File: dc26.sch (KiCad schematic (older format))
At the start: 50 parts, among them J1 CONN_01X10, J2 CONN_01X10, J3 CONN_01X10, Y1 Crystal

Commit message: Pads for unused pins
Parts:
- removed CON_PWR1: CONN_01X02, Pin_Headers:Pin_Header_Angled_1x02_Pitch2.54mm, symbol CONN_01X02
- removed J1, J2: CONN_01X10, Pin_Headers:Pin_Header_Angled_1x10_Pitch2.00mm, symbol CONN_01X10
- added IRRXF1: IRRXF, Measurement_Points:Measurement_Point_Round-SMD-Pad_Small, symbol TEST
- added IRTXF1: IRTXF, Measurement_Points:Measurement_Point_Round-SMD-Pad_Small, symbol TEST
- added PC0: PC0, Measurement_Points:Measurement_Point_Round-SMD-Pad_Small, symbol TEST
- added PC1: PC1, Measurement_Points:Measurement_Point_Round-SMD-Pad_Small, symbol TEST
- added PC12: PC12, Measurement_Points:Measurement_Point_Round-SMD-Pad_Small, symbol TEST
- added PC13: PC13, Measurement_Points:Measurement_Point_Round-SMD-Pad_Small, symbol TEST
- added PC14: PC14, Measurement_Points:Measurement_Point_Round-SMD-Pad_Small, symbol TEST
- added PC15: PC15, Measurement_Points:Measurement_Point_Round-SMD-Pad_Small, symbol TEST
- added PC2: PC2, Measurement_Points:Measurement_Point_Round-SMD-Pad_Small, symbol TEST
- added PC3: PC3, Measurement_Points:Measurement_Point_Round-SMD-Pad_Small, symbol TEST
- added PC4: PC4, Measurement_Points:Measurement_Point_Round-SMD-Pad_Small, symbol TEST
- added PC5: PC5, Measurement_Points:Measurement_Point_Round-SMD-Pad_Small, symbol TEST
- added PC6: PC6, Measurement_Points:Measurement_Point_Round-SMD-Pad_Small, symbol TEST
- added PC7: PC7, Measurement_Points:Measurement_Point_Round-SMD-Pad_Small, symbol TEST
- added PC8: PC8, Measurement_Points:Measurement_Point_Round-SMD-Pad_Small, symbol TEST
- added PC9: PC9, Measurement_Points:Measurement_Point_Round-SMD-Pad_Small, symbol TEST
- SW_BOOT0, SW_RESET1: footprint Buttons_Switches_SMD:SW_SPST_EVQQ2 -> Buttons_Switches_SMD:SW_SPST_EVQPE1
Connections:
- net labels removed: VCC
- wire segments 207 -> 215

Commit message: voltage divider
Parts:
- removed PC12: PC12, Measurement_Points:Measurement_Point_Round-SMD-Pad_Small, symbol TEST
- removed PC13: PC13, Measurement_Points:Measurement_Point_Round-SMD-Pad_Small, symbol TEST
- removed PC14: PC14, Measurement_Points:Measurement_Point_Round-SMD-Pad_Small, symbol TEST
- removed PC15: PC15, Measurement_Points:Measurement_Point_Round-SMD-Pad_Small, symbol TEST
- removed PC9: PC9, Measurement_Points:Measurement_Point_Round-SMD-Pad_Small, symbol TEST
- added C?: 0.1uF, Capacitors_SMD:C_0603, symbol C_Small
- added VBAT-DIV1: 5k-10k, TO_SOT_Packages_SMD:SOT-23, symbol Voltage_Divider
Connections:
- net labels added: +BATT
- wire segments 215 -> 212
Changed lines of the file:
@@
-$EndComp
-$Comp
-L TEST PC9
-U 1 1 5B18EB92
-P -11550 8450
-F 0 "PC9" H -11550 8750 50  0000 C BNN
-F 1 "PC9" H -11550 8700 50  0000 C CNN
-F 2 "Measurement_Points:Measurement_Point_Round-SMD-Pad_Small" H -11550 8450 50  0001 C CNN
-F 3 "" H -11550 8450 50  0001 C CNN
-	1    -11550 8450
-	-1   0    0    1
 $EndComp
 $Comp
@@
 	-1   0    0    1
 $EndComp
-$Comp
-L TEST PC12
-U 1 1 5B18EDE3
-P -12000 8900
-F 0 "PC12" H -12000 9200 50  0000 C BNN
-F 1 "PC12" H -12000 9150 50  0000 C CNN
-F 2 "Measurement_Points:Measurement_Point_Round-SMD-Pad_Small" H -12000 8900 50  0001 C CNN
-F 3 "" H -12000 8900 50  0001 C CNN
-	1    -12000 8900
-	-1   0    0    1
-$EndComp
-$Comp
-L TEST PC13
-U 1 1 5B18EEAC
-P -12150 9050
-F 0 "PC13" H -12150 9350 50  0000 C BNN
-F 1 "PC13" H -12150 9300 50  0000 C CNN
-F 2 "Measurement_Points:Measurement_Point_Round-SMD-Pad_Small" H -12150 9050 50  0001 C CNN
-F 3 "" H -12150 9050 50  0001 C CNN
-	1    -12150 9050
-	-1   0    0    1
-$EndComp
-$Comp
-L TEST PC14
-U 1 1 5B18EF78
-P -12300 9200
-F 0 "PC14" H -12300 9500 50  0000 C BNN
-F 1 "PC14" H -12300 9450 50  0000 C CNN
-F 2 "Measurement_Points:Measurement_Point_Round-SMD-Pad_Small" H -12300 9200 50  0001 C CNN
-F 3 "" H -12300 9200 50  0001 C CNN
-	1    -12300 9200
-	-1   0    0    1
-$EndComp
-$Comp
-L TEST PC15
-U 1 1 5B18F04B
-P -12450 9350
-F 0 "PC15" H -12450 9650 50  0000 C BNN
-F 1 "PC15" H -12450 9600 50  0000 C CNN
-F 2 "Measurement_Points:Measurement_Point_Round-SMD-Pad_Small" H -12450 9350 50  0001 C CNN
-F 3 "" H -12450 9350 50  0001 C CNN
-	1    -12450 9350
-	-1   0    0    1
-$EndComp
 Wire Wire Line
 	-4700 -6350 -3700 -6350
@@
 	-2500 -5700 -3500 -5700
 Wire Wire Line
-	-3500 -4900 -3500 -5700
-Wire Wire Line
-	-4700 -4900 -3500 -4900
+	-3500 -5700 -3500 -4900
+Wire Wire Line
+	-3500 -4900 -4700 -4900
 Wire Wire Line
 	-2500 -5600 -3400 -5600
 Wire Wire Line
-	-3400 -4650 -3400 -5600
-Wire Wire Line
-	-4700 -4650 -3400 -4650
+	-3400 -5600 -3400 -4650
+Wire Wire Line
+	-3400 -4650 -4700 -4650
 Wire Wire Line
 	-2500 -5500 -3350 -5500
 Wire Wire Line
-	-3350 -4400 -3350 -5500
-Wire Wire Line
-	-4700 -4400 -3350 -4400
+	-3350 -5500 -3350 -4400
+Wire Wire Line
+	-3350 -4400 -4700 -4400
 Wire Wire Line
 	-2500 -4650 -3300 -4650
 Wire Wire Line
-	-3300 -4000 -3300 -4650
-Wire Wire Line
-	-4700 -4000 -3300 -4000
+	-3300 -4650 -3300 -4000
+Wire Wire Line
+	-3300 -4000 -4700 -4000
 Wire Wire Line
 	-2500 -4550 -3250 -4550
 Wire Wire Line
-	-3250 -3750 -3250 -4550
-Wire Wire Line
-	-4700 -3750 -3250 -3750
+	-3250 -4550 -3250 -3750
+Wire Wire Line
+	-3250 -3750 -4700 -3750
 Wire Wire Line
 	-5650 -6600 -5650 -3750
@@
 	-2100 6950 -2100 4050
 Wire Wire Line
-	-3050 4050 -2100 4050
-Wire Wire Line
-	-3050 -2850 -3050 4050
-Wire Wire Line
-	-2900 -2850 -3050 -2850
+	-2100 4050 -3050 4050
+Wire Wire Line
+	-3050 4050 -3050 -2850
+Wire Wire Line
+	-3050 -2850 -2900 -2850
 Wire Wire Line
 	-2700 7750 850  7750
@@
 	-11300 5950 -12250 5950
 Wire Wire Line
-	-12250 5850 -12250 5950
-Wire Wire Line
-	-13650 5850 -12250 5850
+	-12250 5950 -12250 5850
+Wire Wire Line
+	-12250 5850 -13650 5850
 Wire Wire Line
 	-11300 6050 -12250 6050
 Wire Wire Line
-	-12250 6150 -12250 6050
-Wire Wire Line
-	-13650 6150 -12250 6150
+	-12250 6050 -12250 6150
+Wire Wire Line
+	-12250 6150 -13650 6150
 Wire Wire Line
 	-13400 6250 -13400 5850
@@
 Connection ~ -11750 7150
 Wire Wire Line
-	-12450 9350 -12450 7950
-Wire Wire Line
-	-12300 9200 -12300 7850
-Connection ~ -12300 7850
-Wire Wire Line
-	-12150 9050 -12150 7750
-Connection ~ -12150 7750
-Wire Wire Line
-	-12000 8900 -12000 7650
-Connection ~ -12000 7650
-Wire Wire Line
 	-11850 8750 -11850 7550
 Connection ~ -11850 7550
 Wire Wire Line
 	-11700 8600 -11700 7450
-Connection ~ -11700 7450
-Wire Wire Line
-	-11550 8450 -11550 7350
-Connection ~ -11550 7350
 Wire Wire Line
 	-11400 8300 -11400 7250
 Connection ~ -11400 7250
+Connection ~ -11700 7450
+$Comp
+L Voltage_Divider VBAT-DIV1
+U 1 1 5B15AEF3
+P -250 6550
+F 0 "VBAT-DIV1" V -425 6550 50  0000 C CNN
+F 1 "5k-10k" V -350 6550 50  0000 C CNN
+F 2 "TO_SOT_Packages_SMD:SOT-23" V 225 6550 50  0001 C CNN
+F 3 "" H -50 6550 50  0001 C CNN
+	1    -250 6550
+	-1   0    0    1
+$EndComp
+Wire Wire Line
+	-2700 6550 -400 6550
+$Comp
+L GND #PWR?
+U 1 1 5B15B26B
+P -250 6800
+F 0 "#PWR?" H -250 6550 50  0001 C CNN
+F 1 "GND" H -250 6650 50  0000 C CNN
+F 2 "" H -250 6800 50  0001 C CNN
+F 3 "" H -250 6800 50  0001 C CNN
+	1    -250 6800
+	1    0    0    -1
+$EndComp
+$Comp
+L +BATT #PWR?
+U 1 1 5B15B508
+P -250 6300
+F 0 "#PWR?" H -250 6150 50  0001 C CNN
+F 1 "+BATT" H -250 6440 50  0000 C CNN
+F 2 "" H -250 6300 50  0001 C CNN
+F 3 "" H -250 6300 50  0001 C CNN
+	1    -250 6300
+	1    0    0    -1
+$EndComp
+$Comp
+L GND #PWR?
+U 1 1 5B15BD01
+P -900 6800
+F 0 "#PWR?" H -900 6550 50  0001 C CNN
+F 1 "GND" H -900 6650 50  0000 C CNN
+F 2 "" H -900 6800 50  0001 C CNN
+F 3 "" H -900 6800 50  0001 C CNN
+	1    -900 6800
+	1    0    0    -1
+$EndComp
+$Comp
+L C_Small C?
+U 1 1 5B15C038
+P -900 6700
+F 0 "C?" H -890 6770 50  0000 L CNN
+F 1 "0.1uF" H -890 6620 50  0000 L CNN
+F 2 "Capacitors_SMD:C_0603" H -900 6700 50  0001 C CNN
+F 3 "" H -900 6700 50  0001 C CNN
+	1    -900 6700
+	1    0    0    -1
+$EndComp
+Wire Wire Line
+	-900 6550 -900 6600
+Connection ~ -900 6550
 $EndSCHEMATC

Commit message: Fixed up some mess + IR + USB new footprint + buttons
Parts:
- removed J3: CONN_01X10, Pin_Headers:Pin_Header_Angled_1x10_Pitch2.00mm, symbol CONN_01X10
- gave numbers to parts that had none: 1
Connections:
- wire segments 212 -> 209
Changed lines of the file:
@@
 $EndComp
 $Comp
-L GND #PWR14
+L GND #PWR12
 U 1 1 5AD27FBE
 P -3450 -6450
-F 0 "#PWR14" H -3450 -6700 50  0001 C CNN
+F 0 "#PWR12" H -3450 -6700 50  0001 C CNN
 F 1 "GND" H -3450 -6600 50  0000 C CNN
 F 2 "" H -3450 -6450 50  0001 C CNN
@@
 $EndComp
 $Comp
-L GND #PWR15
+L GND #PWR13
 U 1 1 5AD6E593
 P -2500 -5100
-F 0 "#PWR15" H -2500 -5350 50  0001 C CNN
+F 0 "#PWR13" H -2500 -5350 50  0001 C CNN
 F 1 "GND" H -2500 -5250 50  0000 C CNN
 F 2 "" H -2500 -5100 50  0001 C CNN
@@
 $EndComp
 $Comp
-L GND #PWR16
+L GND #PWR14
 U 1 1 5AD6F999
 P -2500 -3550
-F 0 "#PWR16" H -2500 -3800 50  0001 C CNN
+F 0 "#PWR14" H -2500 -3800 50  0001 C CNN
 F 1 "GND" H -2500 -3700 50  0000 C CNN
 F 2 "" H -2500 -3550 50  0001 C CNN
@@
 $EndComp
 $Comp
-L GND #PWR13
+L GND #PWR11
 U 1 1 5AD77A72
 P -3600 -800
-F 0 "#PWR13" H -3600 -1050 50  0001 C CNN
+F 0 "#PWR11" H -3600 -1050 50  0001 C CNN
 F 1 "GND" H -3600 -950 50  0000 C CNN
 F 2 "" H -3600 -800 50  0001 C CNN
@@
 $EndComp
 $Comp
-L GND #PWR10
+L GND #PWR8
 U 1 1 5B04F2A2
 P -7000 8800
-F 0 "#PWR10" H -7000 8550 50  0001 C CNN
+F 0 "#PWR8" H -7000 8550 50  0001 C CNN
 F 1 "GND" H -7000 8650 50  0000 C CNN
 F 2 "" H -7000 8800 50  0001 C CNN
@@
 $EndComp
 $Comp
-L +3.3V #PWR9
+L +3.3V #PWR7
 U 1 1 5B0D3E01
 P -7200 2050
-F 0 "#PWR9" H -7200 1900 50  0001 C CNN
+F 0 "#PWR7" H -7200 1900 50  0001 C CNN
 F 1 "+3.3V" H -7200 2190 50  0000 C CNN
 F 2 "" H -7200 2050 50  0001 C CNN
@@
 $EndComp
 $Comp
-L GND #PWR7
+L GND #PWR5
 U 1 1 5B0F137D
 P -12250 5250
-F 0 "#PWR7" H -12250 5000 50  0001 C CNN
+F 0 "#PWR5" H -12250 5000 50  0001 C CNN
 F 1 "GND" H -12250 5100 50  0000 C CNN
 F 2 "" H -12250 5250 50  0001 C CNN
@@
 $EndComp
 $Comp
-L GND #PWR11
+L GND #PWR9
 U 1 1 5B0F6A9C
 P -6200 3750
-F 0 "#PWR11" H -6200 3500 50  0001 C CNN
+F 0 "#PWR9" H -6200 3500 50  0001 C CNN
 F 1 "GND" H -6200 3600 50  0000 C CNN
 F 2 "" H -6200 3750 50  0001 C CNN
@@
 $EndComp
 $Comp
-L +3.3V #PWR8
+L +3.3V #PWR6
 U 1 1 5B11C638
 P -11750 3950
-F 0 "#PWR8" H -11750 3800 50  0001 C CNN
+F 0 "#PWR6" H -11750 3800 50  0001 C CNN
 F 1 "+3.3V" H -11750 4090 50  0000 C CNN
 F 2 "" H -11750 3950 50  0001 C CNN
@@
 $EndComp
 $Comp
-L GND #PWR5
+L GND #PWR4
 U 1 1 5B12677B
 P -12400 4350
-F 0 "#PWR5" H -12400 4100 50  0001 C CNN
+F 0 "#PWR4" H -12400 4100 50  0001 C CNN
 F 1 "GND" H -12400 4200 50  0000 C CNN
 F 2 "" H -12400 4350 50  0001 C CNN
@@
 $EndComp
 $Comp
-L GND #PWR4
+L GND #PWR3
 U 1 1 5B1309D3
 P -12450 4950
-F 0 "#PWR4" H -12450 4700 50  0001 C CNN
+F 0 "#PWR3" H -12450 4700 50  0001 C CNN
 F 1 "GND" H -12450 4800 50  0000 C CNN
 F 2 "" H -12450 4950 50  0001 C CNN
@@
 $EndComp
 $Comp
-L +3.3V #PWR3
+L +3.3V #PWR2
 U 1 1 5B136E3C
 P -12450 4750
-F 0 "#PWR3" H -12450 4600 50  0001 C CNN
+F 0 "#PWR2" H -12450 4600 50  0001 C CNN
 F 1 "+3.3V" H -12450 4890 50  0000 C CNN
 F 2 "" H -12450 4750 50  0001 C CNN
@@
 $EndComp
 $Comp
-L GND #PWR17
+L GND #PWR15
 U 1 1 5B13B631
 P -1800 6650
-F 0 "#PWR17" H -1800 6400 50  0001 C CNN
+F 0 "#PWR15" H -1800 6400 50  0001 C CNN
 F 1 "GND" H -1800 6500 50  0000 C CNN
 F 2 "" H -1800 6650 50  0001 C CNN
@@
 $EndComp
 $Comp
-L GND #PWR18
+L GND #PWR16
 U 1 1 5B1B7467
 P -1200 9050
-F 0 "#PWR18" H -1200 8800 50  0001 C CNN
+F 0 "#PWR16" H -1200 8800 50  0001 C CNN
 F 1 "GND" H -1200 8900 50  0000 C CNN
 F 2 "" H -1200 9050 50  0001 C CNN
@@
 $EndComp
 $Comp
-L +5V #PWR12
+L +5V #PWR10
 U 1 1 5B123F56
 P -5650 -6600
-F 0 "#PWR12" H -5650 -6750 50  0001 C CNN
+F 0 "#PWR10" H -5650 -6750 50  0001 C CNN
 F 1 "+5V" H -5650 -6460 50  0000 C CNN
 F 2 "" H -5650 -6600 50  0001 C CNN
@@
 LED-POWER-ENABLE
 $Comp
-L GND #PWR22
+L GND #PWR20
 U 1 1 5B188D2F
 P -1100 -5650
-F 0 "#PWR22" H -1100 -5900 50  0001 C CNN
+F 0 "#PWR20" H -1100 -5900 50  0001 C CNN
 F 1 "GND" H -1100 -5800 50  0000 C CNN
 F 2 "" H -1100 -5650 50  0001 C CNN
@@
 $EndComp
 $Comp
-L +5V #PWR21
+L +5V #PWR19
 U 1 1 5B1896AE
 P -1100 -5850
-F 0 "#PWR21" H -1100 -6000 50  0001 C CNN
+F 0 "#PWR19" H -1100 -6000 50  0001 C CNN
 F 1 "+5V" H -1100 -5710 50  0000 C CNN
 F 2 "" H -1100 -5850 50  0001 C CNN
@@
 $EndComp
 $Comp
-L +5V #PWR19
+L +5V #PWR17
 U 1 1 5B189C3C
 P -1150 -4300
-F 0 "#PWR19" H -1150 -4450 50  0001 C CNN
+F 0 "#PWR17" H -1150 -4450 50  0001 C CNN
 F 1 "+5V" H -1150 -4160 50  0000 C CNN
 F 2 "" H -1150 -4300 50  0001 C CNN
@@
 $EndComp
 $Comp
-L GND #PWR20
+L GND #PWR18
 U 1 1 5B189D37
 P -1150 -4150
-F 0 "#PWR20" H -1150 -4400 50  0001 C CNN
+F 0 "#PWR18" H -1150 -4400 50  0001 C CNN
 F 1 "GND" H -1150 -4300 50  0000 C CNN
 F 2 "" H -1150 -4150 50  0001 C CNN
@@
 IR-TX-F
 $Comp
-L CONN_01X10 J3
-U 1 1 5B13C46C
-P 1050 7500
-F 0 "J3" H 1050 8050 50  0000 C CNN
-F 1 "CONN_01X10" V 1150 7500 50  0000 C CNN
-F 2 "Pin_Headers:Pin_Header_Angled_1x10_Pitch2.00mm" H 1050 7500 50  0001 C CNN
-F 3 "" H 1050 7500 50  0001 C CNN
-	1    1050 7500
-	1    0    0    -1
-$EndComp
-$Comp
 L TEST PC0
 U 1 1 5B18C803
@@
 	-13250 7450 -11300 7450
 Wire Wire Line
-	-2700 7850 850  7850
-Wire Wire Line
-	-2700 7650 850  7650
-Wire Wire Line
 	-2700 7550 850  7550
 Wire Wire Line
 	-2700 7450 850  7450
-Wire Wire Line
-	-2700 7350 850  7350
 Wire Wire Line
 	-2700 7250 850  7250
@@
 	-2700 6550 -400 6550
 $Comp
-L GND #PWR?
+L GND #PWR23
 U 1 1 5B15B26B
 P -250 6800
-F 0 "#PWR?" H -250 6550 50  0001 C CNN
+F 0 "#PWR23" H -250 6550 50  0001 C CNN
 F 1 "GND" H -250 6650 50  0000 C CNN
 F 2 "" H -250 6800 50  0001 C CNN
@@
 $EndComp
 $Comp
-L +BATT #PWR?
+L +BATT #PWR22
 U 1 1 5B15B508
 P -250 6300
-F 0 "#PWR?" H -250 6150 50  0001 C CNN
+F 0 "#PWR22" H -250 6150 50  0001 C CNN
 F 1 "+BATT" H -250 6440 50  0000 C CNN
 F 2 "" H -250 6300 50  0001 C CNN
@@
 $EndComp
 $Comp
-L GND #PWR?
+L GND #PWR21
 U 1 1 5B15BD01
 P -900 6800
-F 0 "#PWR?" H -900 6550 50  0001 C CNN
+F 0 "#PWR21" H -900 6550 50  0001 C CNN
 F 1 "GND" H -900 6650 50  0000 C CNN
 F 2 "" H -900 6800 50  0001 C CNN
@@
 $EndComp
 $Comp
-L C_Small C?
+L C_Small C2
 U 1 1 5B15C038
 P -900 6700
-F 0 "C?" H -890 6770 50  0000 L CNN
+F 0 "C2" H -890 6770 50  0000 L CNN
 F 1 "0.1uF" H -890 6620 50  0000 L CNN
 F 2 "Capacitors_SMD:C_0603" H -900 6700 50  0001 C CNN

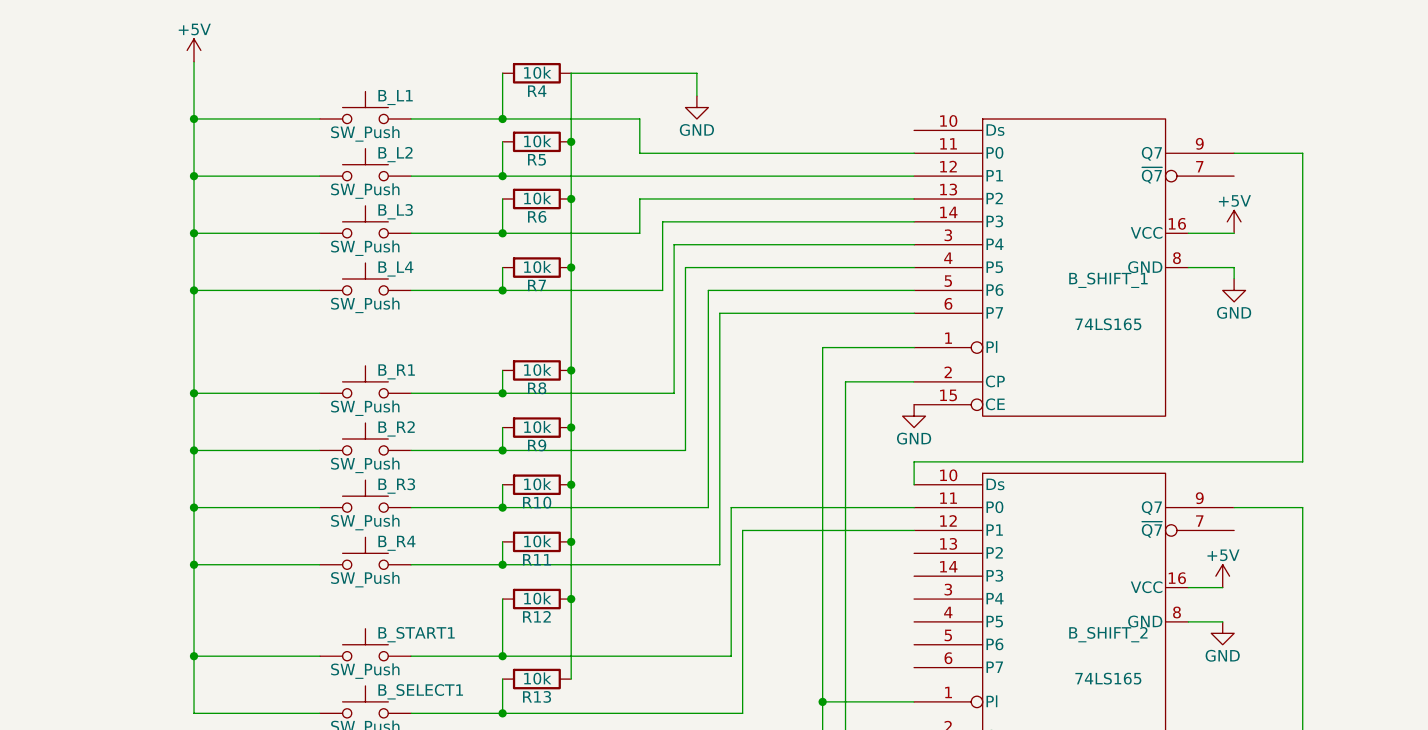
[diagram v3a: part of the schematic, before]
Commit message: clean up and moved shifters to 3.3v
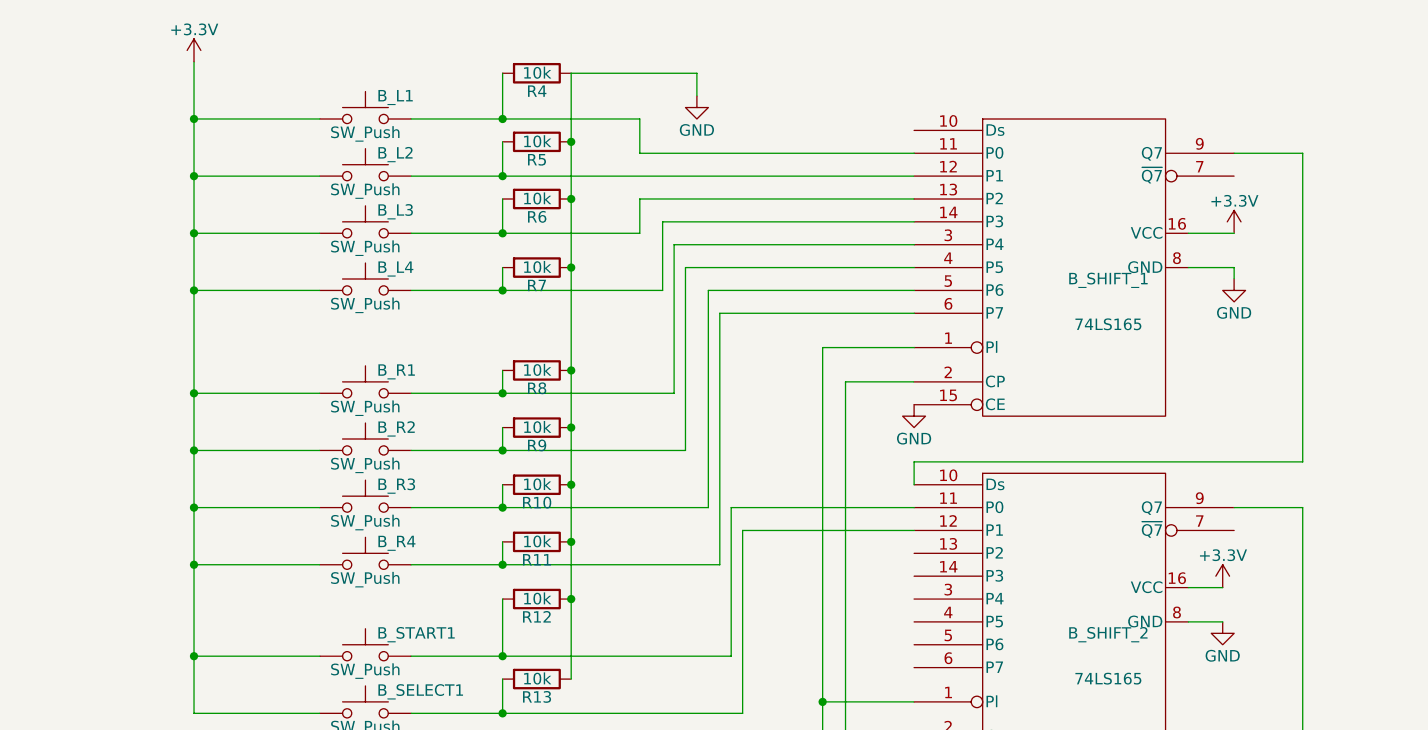
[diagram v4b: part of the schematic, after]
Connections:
- net labels removed: +5V
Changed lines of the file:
@@
 	0    1    1    0
-$EndComp
-$Comp
-L +5V #PWR10
-U 1 1 5B123F56
-P -5650 -6600
-F 0 "#PWR10" H -5650 -6750 50  0001 C CNN
-F 1 "+5V" H -5650 -6460 50  0000 C CNN
-F 2 "" H -5650 -6600 50  0001 C CNN
-F 3 "" H -5650 -6600 50  0001 C CNN
-	1    -5650 -6600
-	1    0    0    -1
 $EndComp
 Text GLabel -1550 6250 2    60   Input ~ 0
@@
 F 3 "" H -1800 -5700 50  0001 C CNN
 	1    -1800 -5700
-	1    0    0    -1
-$EndComp
-$Comp
-L +5V #PWR19
-U 1 1 5B1896AE
-P -1100 -5850
-F 0 "#PWR19" H -1100 -6000 50  0001 C CNN
-F 1 "+5V" H -1100 -5710 50  0000 C CNN
-F 2 "" H -1100 -5850 50  0001 C CNN
-F 3 "" H -1100 -5850 50  0001 C CNN
-	1    -1100 -5850
-	1    0    0    -1
-$EndComp
-$Comp
-L +5V #PWR17
-U 1 1 5B189C3C
-P -1150 -4300
-F 0 "#PWR17" H -1150 -4450 50  0001 C CNN
-F 1 "+5V" H -1150 -4160 50  0000 C CNN
-F 2 "" H -1150 -4300 50  0001 C CNN
-F 3 "" H -1150 -4300 50  0001 C CNN
-	1    -1150 -4300
 	1    0    0    -1
 $EndComp
@@
 	-900 6550 -900 6600
 Connection ~ -900 6550
+$Comp
+L +3.3V #PWR?
+U 1 1 5B17BB18
+P -5650 -6600
+F 0 "#PWR?" H -5650 -6750 50  0001 C CNN
+F 1 "+3.3V" H -5650 -6460 50  0000 C CNN
+F 2 "" H -5650 -6600 50  0001 C CNN
+F 3 "" H -5650 -6600 50  0001 C CNN
+	1    -5650 -6600
+	1    0    0    -1
+$EndComp
+$Comp
+L +3.3V #PWR?
+U 1 1 5B17C07B
+P -1100 -5850
+F 0 "#PWR?" H -1100 -6000 50  0001 C CNN
+F 1 "+3.3V" H -1100 -5710 50  0000 C CNN
+F 2 "" H -1100 -5850 50  0001 C CNN
+F 3 "" H -1100 -5850 50  0001 C CNN
+	1    -1100 -5850
+	1    0    0    -1
+$EndComp
+$Comp
+L +3.3V #PWR?
+U 1 1 5B17C77B
+P -1150 -4300
+F 0 "#PWR?" H -1150 -4450 50  0001 C CNN
+F 1 "+3.3V" H -1150 -4160 50  0000 C CNN
+F 2 "" H -1150 -4300 50  0001 C CNN
+F 3 "" H -1150 -4300 50  0001 C CNN
+	1    -1150 -4300
+	1    0    0    -1
+$EndComp
 $EndSCHEMATC
